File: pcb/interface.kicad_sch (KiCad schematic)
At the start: 23 parts, among them J10 Power Out, J2 QWICC, J5 QWICC, J7 Power In, J9 AVR-UPDI-6

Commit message: Standardized parts; fixed title box
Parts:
- J8: Mouser (none) -> 306-BM03BSRSSTBLFSNP
- TP10, TP11, TP12, TP4, TP5, TP6, TP7, TP8, TP9: now left out of the parts list
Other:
- title: Relay Module -> Servo Module
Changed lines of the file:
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@@
 	(paper "A4")
 	(title_block
-		(title "Relay Module")
+		(title "Servo Module")
 		(date "<<release-date>>")
 		(rev "<<tag>>")
@@
 		(unit 1)
 		(exclude_from_sim no)
-		(in_bom yes)
+		(in_bom no)
 		(on_board yes)
 		(dnp no)
@@
 		(unit 1)
 		(exclude_from_sim no)
-		(in_bom yes)
+		(in_bom no)
 		(on_board yes)
 		(dnp no)
@@
 		(unit 1)
 		(exclude_from_sim no)
-		(in_bom yes)
+		(in_bom no)
 		(on_board yes)
 		(dnp no)
@@
 			)
 		)
-		(property "Datasheet" ""
+		(property "Datasheet" "https://www.jst-mfg.com/product/pdf/eng/eSH.pdf"
 			(at 59.69 90.17 0)
 			(effects
@@
 			)
 		)
-		(property "Datasheet" ""
+		(property "Datasheet" "https://www.jst-mfg.com/product/pdf/eng/eSH.pdf"
 			(at 59.69 69.85 0)
 			(effects
@@
 		(unit 1)
 		(exclude_from_sim no)
-		(in_bom yes)
+		(in_bom no)
 		(on_board yes)
 		(dnp no)
@@
 			)
 		)
-		(property "Datasheet" ""
+		(property "Datasheet" "https://www.jst-mfg.com/product/pdf/eng/eSH.pdf"
 			(at 59.69 25.4 0)
 			(effects
@@
 			)
 		)
-		(property "Datasheet" ""
+		(property "Datasheet" "https://www.jst-mfg.com/product/pdf/eng/eSH.pdf"
 			(at 59.69 46.99 0)
 			(effects
@@
 			)
 		)
-		(property "Datasheet" ""
+		(property "Datasheet" "https://www.jst-mfg.com/product/pdf/eng/eSH.pdf"
 			(at 91.44 83.82 0)
 			(effects
@@
 		(unit 1)
 		(exclude_from_sim no)
-		(in_bom yes)
+		(in_bom no)
 		(on_board yes)
 		(dnp no)
@@
 			)
 		)
-		(property "Datasheet" ""
+		(property "Datasheet" "https://www.jst-mfg.com/product/pdf/eng/eSH.pdf"
 			(at 91.44 33.02 0)
 			(effects
@@
 		(unit 1)
 		(exclude_from_sim no)
-		(in_bom yes)
+		(in_bom no)
 		(on_board yes)
 		(dnp no)
@@
 		(unit 1)
 		(exclude_from_sim no)
-		(in_bom yes)
+		(in_bom no)
 		(on_board yes)
 		(dnp no)
@@
 			)
 		)
-		(property "Datasheet" ""
+		(property "Datasheet" "https://www.jst-mfg.com/product/pdf/eng/eSH.pdf"
 			(at 203.2 35.56 0)
 			(effects
@@
 			)
 		)
-		(property "Mouser" ""
+		(property "Mouser" "306-BM03BSRSSTBLFSNP"
 			(at 203.2 35.56 0)
 			(effects
@@
 		(unit 1)
 		(exclude_from_sim no)
-		(in_bom yes)
+		(in_bom no)
 		(on_board yes)
 		(dnp no)
@@
 		(unit 1)
 		(exclude_from_sim no)
-		(in_bom yes)
+		(in_bom no)
 		(on_board yes)
 		(dnp no)

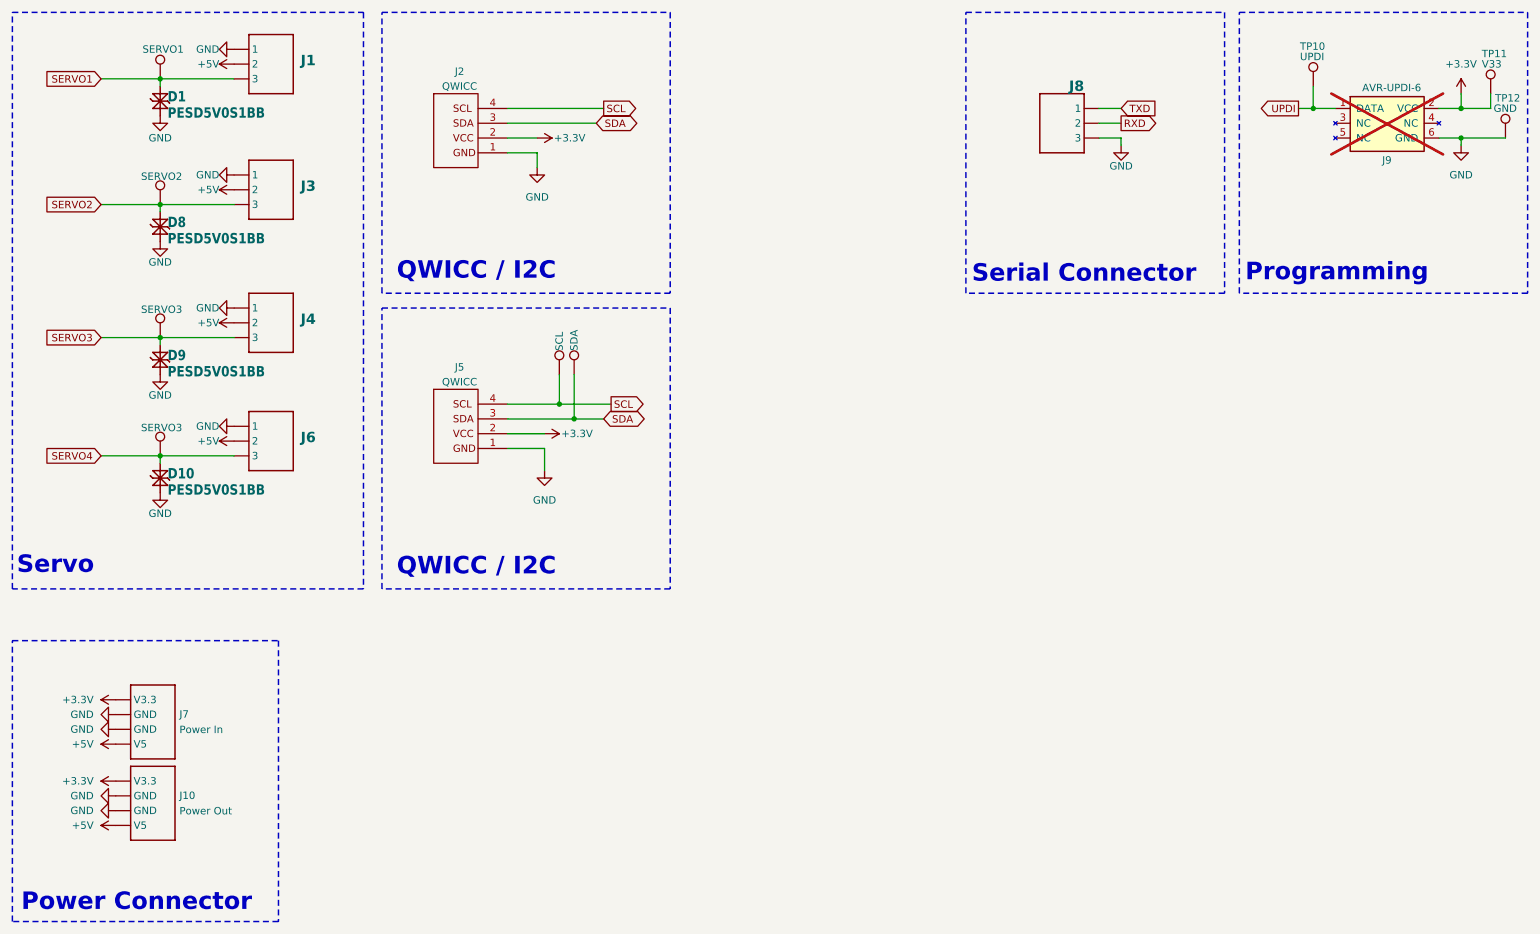
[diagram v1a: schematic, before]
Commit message: Reworked based on new standards
Decreased to 3 servo ports
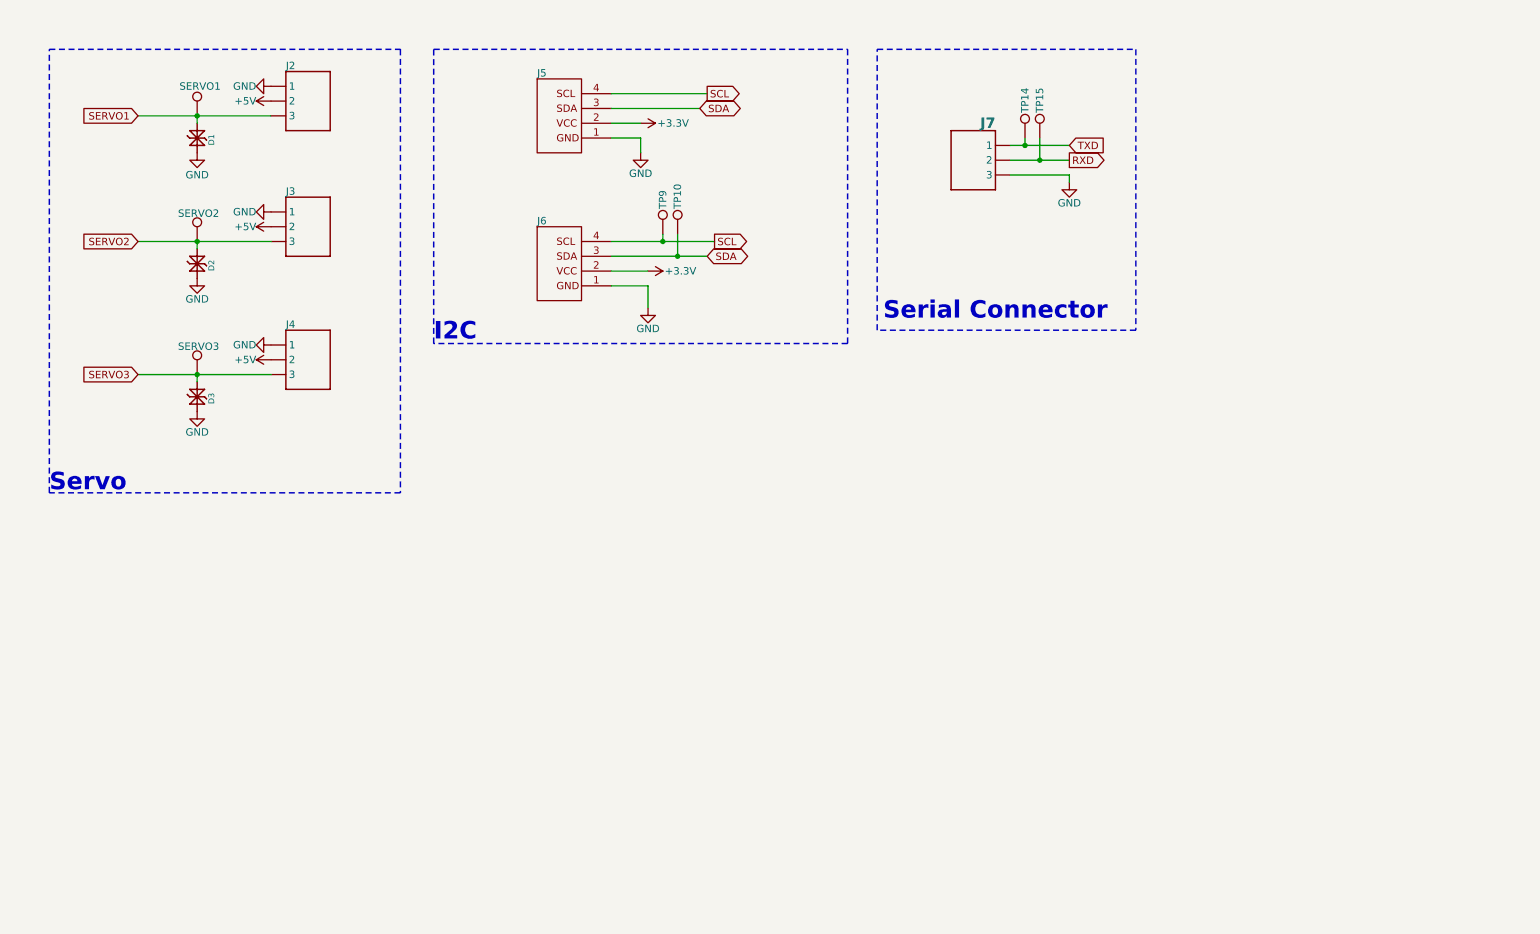
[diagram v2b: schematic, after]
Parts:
- removed D1, D10, D8, D9: PESD5V0S1BB, CRGM Passive:D_SOD-523, symbol CRGM Passive:PESD5V0S1BB
- removed J1, J6: ~, CRGM Connector:JST_SH_BM03B-SRSS-TB_1x03-1MP_P1.00mm_Vertical, symbol CRGM Connector:JST-SH-3
- removed J10: Power Out, CRGM Connector:JST_SH_SM04B-SRSS-TB_1x04-1MP_P1.00mm_Horizontal, symbol CRGM Connector:AQ_POWER
- removed J2: QWICC, CRGM Connector:JST_SH_SM04B-SRSS-TB_1x04-1MP_P1.00mm_Horizontal, symbol CRGM Connector:QWIIC
- removed J7: Power In, CRGM Connector:JST_SH_SM04B-SRSS-TB_1x04-1MP_P1.00mm_Horizontal, symbol CRGM Connector:AQ_POWER
- removed J9: AVR-UPDI-6, CRGM Connector:PinHeader_2x03_P2.54mm_Vertical_SMD, symbol CRGM Connector:AVR-UPDI-6
- removed TP10: UPDI, CRGM Mechanical:TestPoint_Pad_D1.0mm, symbol Connector:TestPoint
- removed TP11: V33, CRGM Mechanical:TestPoint_Pad_D1.0mm, symbol Connector:TestPoint
- removed TP12: GND, CRGM Mechanical:TestPoint_Pad_D1.0mm, symbol Connector:TestPoint
- removed TP9: SERVO3, CRGM Mechanical:TestPoint_Pad_D1.0mm, symbol Connector:TestPoint
- added D1, D2, D3: PESD5V5C1BL, CRGM Passive:DFN1006-2, symbol CRGM Passive:PESD5V5C1BLYL
- added J2: ~, CRGM Connector:JST_SH_BM03B-SRSS-TB_1x03-1MP_P1.00mm_Vertical, symbol CRGM Connector:JST-SH-3
- added J6: ~, CRGM Connector:JST_SH_SM04B-SRSS-TB_1x04-1MP_P1.00mm_Horizontal, symbol CRGM Connector:QWIIC
- added TP14, TP15: ~, CRGM Mechanical:TestPoint_Pad_D1.0mm, symbol Connector:TestPoint
- J3, J4: Digikey 455-BM03B-SRSS-TBTR-ND -> 455-BM04B-SRSS-TBTR-ND; LCSC C2919600 -> C2919601; MPN BM03B-SRSS-TB -> BM04B-SRSS-TB; Mouser 306-BM03BSRSSTBLFSNP -> 306-BM04BSRSSTBTLFSN
- J5: value QWICC -> ~; Digikey 455-SM04B-SRSS-TBTR-ND -> 455-BM04B-SRSS-TBTR-ND; Mouser 306-SM04BSRSSTBTLFSN -> 306-BM04BSRSSTBTLFSN
- J7: renamed from J8; Digikey (none) -> 455-BM04B-SRSS-TBTR-ND; LCSC C2919600 -> C2919601; MPN BM03B-SRSS-TB -> BM04B-SRSS-TB; Mouser 306-BM03BSRSSTBLFSNP -> 306-BM04BSRSSTBTLFSN
- TP10: renamed from TP8; value SDA -> ~
- TP9: renamed from TP7; value SCL -> ~
- renumbered TP4 to TP6, TP5 to TP7, TP6 to TP8
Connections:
- net +3.3V: now also J6.2
- net +5V: now also J2.2
- net GND: now also D1.1 (K1), D2.1 (K1), D3.1 (K1), J2.1, J6.1
- net RXD: now also TP15.1
- net SCL: now also J6.4
- net SDA: now also J6.3
- net SERVO1: now also D1.2 (K2), J2.3
- net SERVO2: now also D2.2 (K2)
- net SERVO3: now also D3.2 (K2)
- net TXD: now also TP14.1
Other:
- note added: "I2C"
- note removed: "Power Connector"
- note removed: "Programming"
- note removed: "QWICC / I2C"
- moved on the sheet: J7

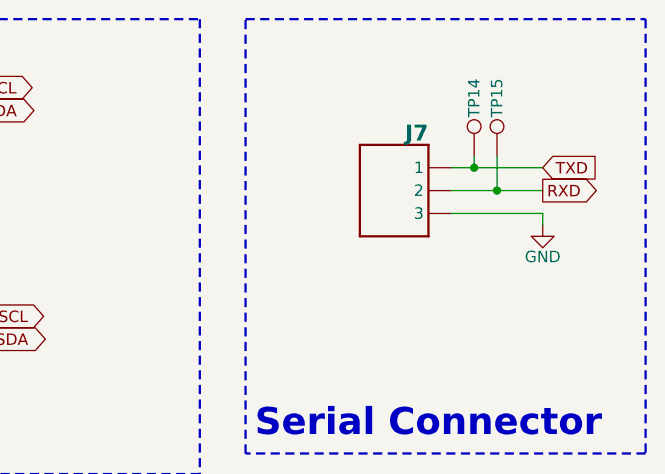
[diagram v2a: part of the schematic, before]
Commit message: Fixed connector to be horizontal
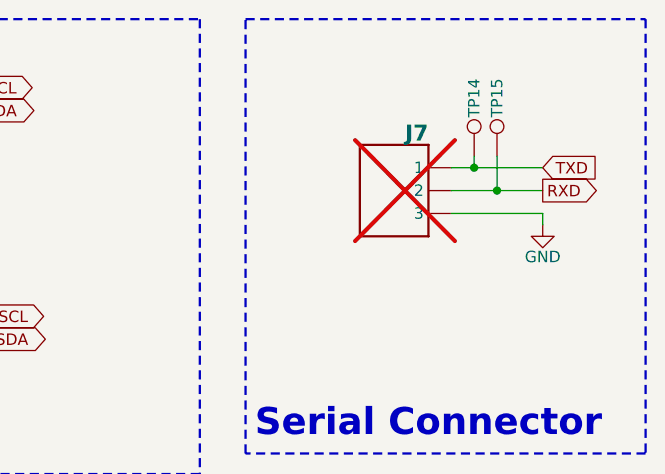
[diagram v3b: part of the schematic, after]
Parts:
- J2, J3, J4: footprint CRGM Connector:JST_SH_BM03B-SRSS-TB_1x03-1MP_P1.00mm_Vertical -> CRGM Connector:JST_SH_SM03B-SRSS-TB_1x03-1MP_P1.00mm_Horizontal; Digikey 455-BM04B-SRSS-TBTR-ND -> 455-SM03B-SRSS-TBTR-ND; LCSC C2919601 -> C2763613; MPN BM04B-SRSS-TB -> SM03B-SRSS-TB; Mouser 306-BM04BSRSSTBTLFSN -> 306-SM03BSRSSTBTLFSN
- J7: now not fitted; now left out of the parts list

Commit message: Added servo power and filtering
Added connection for servo power
Added solder jumper for servo power to 5V
Added caps to servo power
Added bulk decoupling caps
Added TVS to various inputs
Updated renders
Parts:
- removed D1, D2, D3: PESD5V5C1BL, CRGM Passive:DFN1006-2, symbol CRGM Passive:PESD5V5C1BLYL
- added C2: 0.1uF, CRGM Passive:C_0603_1608Metric, symbol Device:C_Small
- added C3: 100uF, CRGM Passive:CP_Elec_5x5.4, symbol CRGM Passive:C_Polarized_Small
- added D4: PESD5V5C1BL, CRGM Passive:DFN1006-2, symbol CRGM Passive:PESD5V5C1BLYL
- added D5, D6, D7: PESD3V3S1BL, CRGM Passive:DFN1006-2, symbol CRGM Passive:PESD3V3S1BL
- added J5: ~, CRGM Connector:JST_SH_SM02B-SRSS-TB_1x02-1MP_P1.00mm_Horizontal, symbol CRGM Connector:JST-SH-2
- added JP5: ~, CRGM Connector:SolderJumper-2_P2.0mm_Bridged_RoundedPad1.0x1.5mm, symbol Jumper:SolderJumper_2_Bridged
- renumbered J5 to J6, J6 to J7, J7 to J8, TP9 to TP10, TP10 to TP11, TP14 to TP12, TP15 to TP13, TP6 to TP7, TP7 to TP8, TP8 to TP9
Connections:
- net +5V: now also JP5.1 (A); no longer J2.2, J3.2, J4.2
- net GND: now also C2.2, C3.2, D4.1 (K1), D5.1 (K1), D6.1 (K1), D7.1 (K1), J5.1
- net SERVO1: now also D5.2 (K2)
- net SERVO2: now also D6.2 (K2)
- net SERVO3: now also D7.2 (K2)
- new net VSERVO: C2.1, C3.1, D4.2 (K2), J2.2, J3.2, J4.2, J5.2, JP5.2 (B)

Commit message: Adjusting back on lessons learned from 1.1,
Added skilkscreen
Moved UART to UPDI connector
Created room for 4th servo connector?
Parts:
- removed J8: ~, CRGM Connector:JST_SH_BM03B-SRSS-TB_1x03-1MP_P1.00mm_Vertical, symbol CRGM Connector:JST-SH-3
- removed TP12, TP13: ~, CRGM Mechanical:TestPoint_Pad_D1.0mm, symbol Connector:TestPoint
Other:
- note removed: "Serial Connector"

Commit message: changed connectors to vertical
Updated connectors with ground on mounting points
Updated and rerouted
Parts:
- added D13: PESD3V3S1BL, CRGM Passive:DFN1006-2, symbol CRGM Passive:PESD3V3S1BL
- added J8: ~, CRGM Connector:JST_SH_BM03B-SRSS-TB_1x03-1MP_P1.00mm_Vertical, symbol CRGM Connector:JST-SH-3
- added TP12: SERVO4, CRGM Mechanical:TestPoint_Pad_D1.0mm, symbol Connector:TestPoint
- J2, J3, J4: footprint CRGM Connector:JST_SH_SM03B-SRSS-TB_1x03-1MP_P1.00mm_Horizontal -> CRGM Connector:JST_SH_BM03B-SRSS-TB_1x03-1MP_P1.00mm_Vertical; Digikey 455-SM03B-SRSS-TBTR-ND -> 455-BM04B-SRSS-TBTR-ND; LCSC C2763613 -> C2919601; MPN SM03B-SRSS-TB -> BM04B-SRSS-TB; Mouser 306-SM03BSRSSTBTLFSN -> 306-BM04BSRSSTBTLFSN
- J5: footprint CRGM Connector:JST_SH_SM02B-SRSS-TB_1x02-1MP_P1.00mm_Horizontal -> Connector_JST:JST_SH_BM02B-SRSS-TB_1x02-1MP_P1.00mm_Vertical; Digikey 455-SM02B-SRSS-TBTR-ND -> 455-1788-2-ND; MPN SM02B-SRSS-TB -> BM02B-SRSS-TB; Mouser 306-SM02BSRSSTBLFSN -> 306-BM02BSRSSTBLFSNP
- J6: footprint CRGM Connector:JST_SH_SM04B-SRSS-TB_1x04-1MP_P1.00mm_Horizontal -> CRGM Connector:JST_SH_BM04B-SRSS-TB_1x04-1MP_P1.00mm_Vertical; LCSC C2763614 -> C2919601; MPN SM04B-SRSS-TBT(LF)(SN) -> BM04B-SRSS-TBT(LF)(SN)
- J7: footprint CRGM Connector:JST_SH_SM04B-SRSS-TB_1x04-1MP_P1.00mm_Horizontal -> CRGM Connector:JST_SH_BM04B-SRSS-TB_1x04-1MP_P1.00mm_Vertical; Digikey 455-SM04B-SRSS-TBTR-ND -> 455-BM04B-SRSS-TBTR-ND; LCSC C2763614 -> C2919601; MPN SM04B-SRSS-TBT(LF)(SN) -> BM04B-SRSS-TBT(LF)(SN); Mouser 306-SM04BSRSSTBTLFSN -> 306-BM04BSRSSTBTLFSN
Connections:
- net GND: now also J2.0 (MP), J2.4 (MP), J3.0 (MP), J3.4 (MP), J4.0 (MP), J4.4 (MP), J5.0 (MP), J5.3 (MP), J6.0 (MP), J6.5 (MP), J7.0 (MP), J7.5 (MP), D13.1 (K1), J8.0 (MP), J8.1, J8.4 (MP)
- net VSERVO: now also J8.2
- new net SERVO4: D13.2 (K2), J8.3, TP12.1
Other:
- moved on the sheet: C2, C3, D4, JP5

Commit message: Updated more models
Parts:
- J5: footprint Connector_JST:JST_SH_BM02B-SRSS-TB_1x02-1MP_P1.00mm_Vertical -> CRGM Connector:JST_SH_BM02B-SRSS-TB_1x02-1MP_P1.00mm_Vertical
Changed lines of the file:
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@@
 			)
 		)
-		(property "Footprint" "Connector_JST:JST_SH_BM02B-SRSS-TB_1x02-1MP_P1.00mm_Vertical"
+		(property "Footprint" "CRGM Connector:JST_SH_BM02B-SRSS-TB_1x02-1MP_P1.00mm_Vertical"
 			(at 67.31 110.49 0)
 			(effects
